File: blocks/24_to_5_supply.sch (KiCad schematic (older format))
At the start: 9 parts

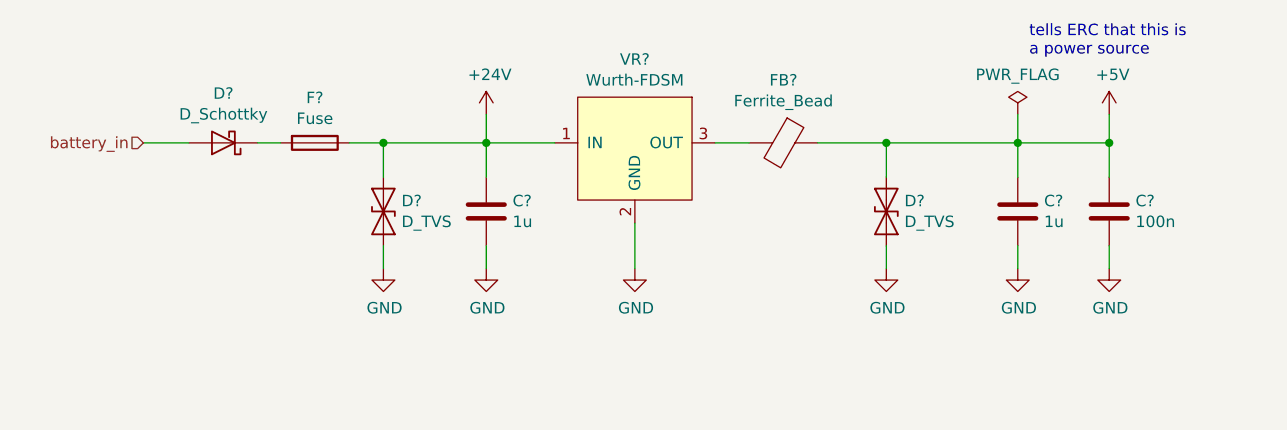
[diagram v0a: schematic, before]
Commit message: changes on blocks
- added led in power supply
- added wurth led driver
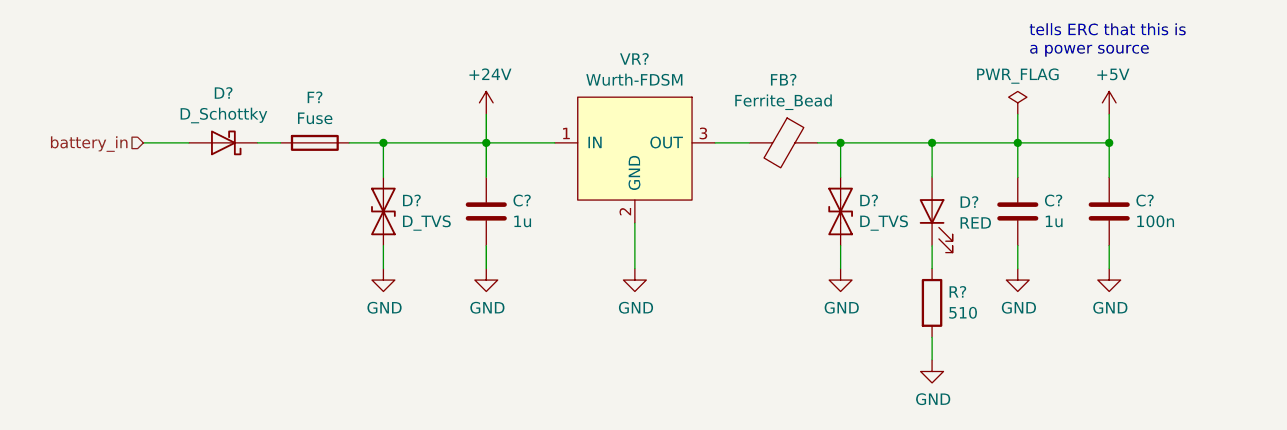
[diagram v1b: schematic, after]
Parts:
- added D?: RED, symbol Device:LED
- added R?: 510, symbol Device:R
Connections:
- net +5V: now also D?.2 (A)
- net GND: now also R?.2
- new net: D?.1 (K), R?.1
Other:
- moved on the sheet: D?
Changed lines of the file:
@@
 L Device:D_TVS D?
 U 1 1 5DE95FEA
-P 6800 3525
-F 0 "D?" V 6754 3604 50  0000 L CNN
-F 1 "D_TVS" V 6845 3604 50  0000 L CNN
-F 2 "" H 6800 3525 50  0001 C CNN
-F 3 "~" H 6800 3525 50  0001 C CNN
-	1    6800 3525
+P 6600 3525
+F 0 "D?" V 6554 3604 50  0000 L CNN
+F 1 "D_TVS" V 6645 3604 50  0000 L CNN
+F 2 "" H 6600 3525 50  0001 C CNN
+F 3 "~" H 6600 3525 50  0001 C CNN
+	1    6600 3525
 	0    1    1    0
 $EndComp
 Wire Wire Line
-	6800 3375 6800 3225
+	6600 3375 6600 3225
 $Comp
 L Device:C C?
@@
 Wire Wire Line
 	7375 3375 7375 3225
-Wire Wire Line
-	7375 3225 6800 3225
-Connection ~ 6800 3225
 $Comp
 L power:+24V #PWR?
@@
 L power:GND #PWR?
 U 1 1 5DE9A361
-P 6800 3775
-F 0 "#PWR?" H 6800 3525 50  0001 C CNN
-F 1 "GND" H 6805 3602 50  0000 C CNN
-F 2 "" H 6800 3775 50  0001 C CNN
-F 3 "" H 6800 3775 50  0001 C CNN
-	1    6800 3775
+P 6600 3775
+F 0 "#PWR?" H 6600 3525 50  0001 C CNN
+F 1 "GND" H 6605 3602 50  0000 C CNN
+F 2 "" H 6600 3775 50  0001 C CNN
+F 3 "" H 6600 3775 50  0001 C CNN
+	1    6600 3775
 	1    0    0    -1
 $EndComp
 Wire Wire Line
-	6800 3775 6800 3675
+	6600 3775 6600 3675
 $Comp
 L power:GND #PWR?
@@
 	6050 3225 6200 3225
 Wire Wire Line
-	6500 3225 6800 3225
+	6500 3225 6600 3225
+Connection ~ 6600 3225
+Wire Wire Line
+	6600 3225 7000 3225
+$Comp
+L Device:LED D?
+U 1 1 5DEA538C
+P 7000 3525
+F 0 "D?" V 7039 3407 50  0000 R CNN
+F 1 "RED" V 6948 3407 50  0000 R CNN
+F 2 "" H 7000 3525 50  0001 C CNN
+F 3 "~" H 7000 3525 50  0001 C CNN
+	1    7000 3525
+	0    -1   -1   0
+$EndComp
+$Comp
+L Device:R R?
+U 1 1 5DEA6286
+P 7000 3925
+F 0 "R?" H 7070 3971 50  0000 L CNN
+F 1 "510" H 7070 3880 50  0000 L CNN
+F 2 "" V 6930 3925 50  0001 C CNN
+F 3 "~" H 7000 3925 50  0001 C CNN
+	1    7000 3925
+	1    0    0    -1
+$EndComp
+Wire Wire Line
+	7000 3375 7000 3225
+Connection ~ 7000 3225
+Wire Wire Line
+	7000 3225 7375 3225
+Wire Wire Line
+	7000 3675 7000 3775
+$Comp
+L power:GND #PWR?
+U 1 1 5DEA756F
+P 7000 4175
+F 0 "#PWR?" H 7000 3925 50  0001 C CNN
+F 1 "GND" H 7005 4002 50  0000 C CNN
+F 2 "" H 7000 4175 50  0001 C CNN
+F 3 "" H 7000 4175 50  0001 C CNN
+	1    7000 4175
+	1    0    0    -1
+$EndComp
+Wire Wire Line
+	7000 4175 7000 4075
 $EndSCHEMATC
